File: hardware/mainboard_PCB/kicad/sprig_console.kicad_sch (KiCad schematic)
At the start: 25 parts, among them J1 1020_battery_holder, J2 Conn_PinHeader_2x03_P2.54mm_V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, SW1 W, SW2 A, SW3 S, SW4 D, SW5 I, SW6 J, SW7 K, SW8 L, SW9 Slideswitch, U2 MAX98357AETE+, U5 Pico

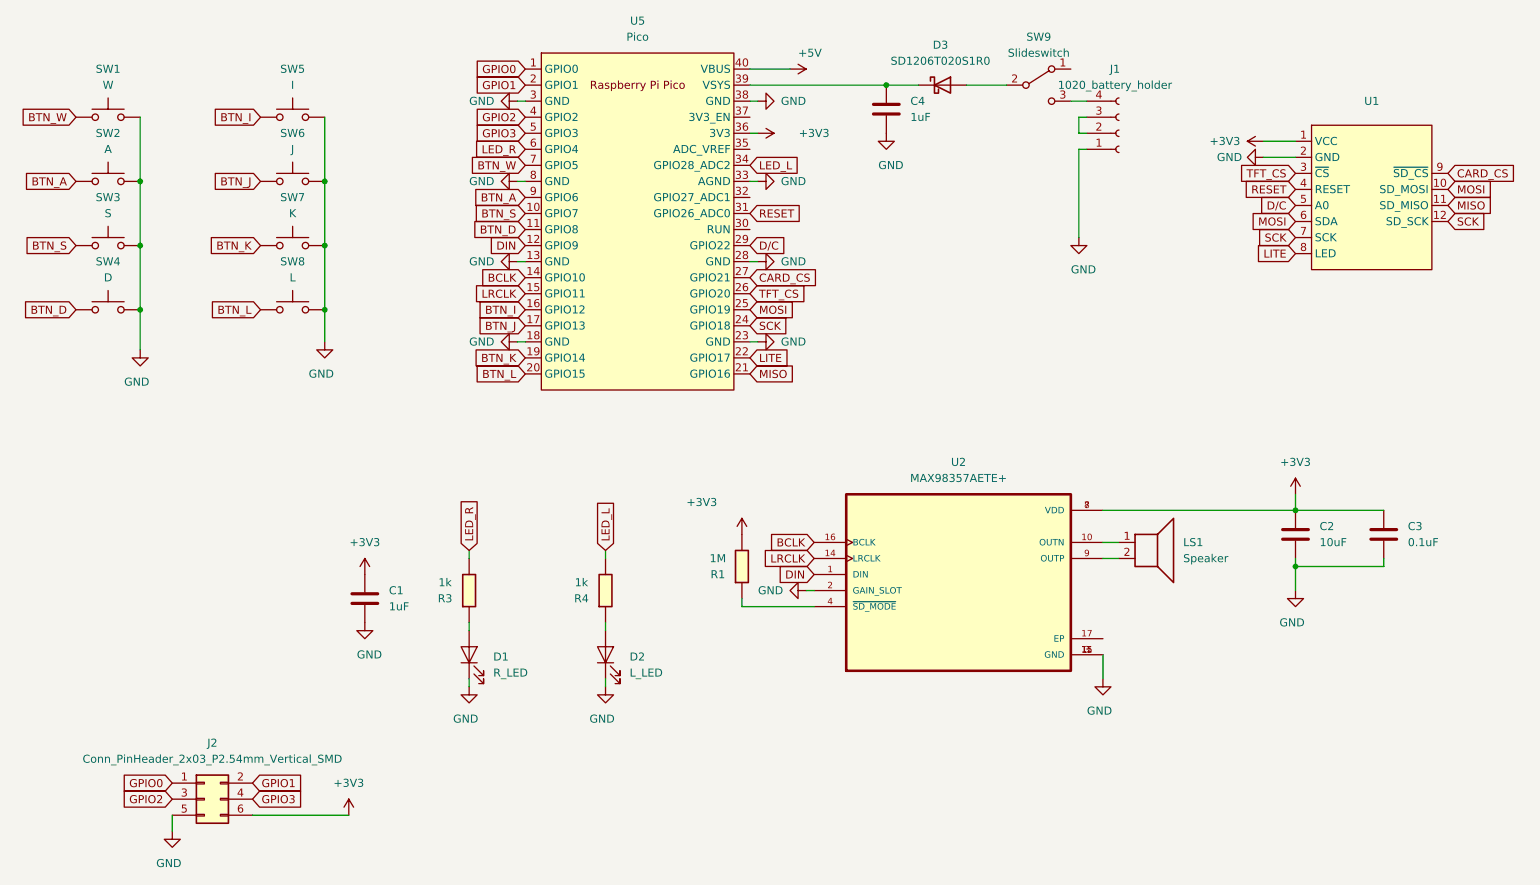
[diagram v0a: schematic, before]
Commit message: temp under screen headers
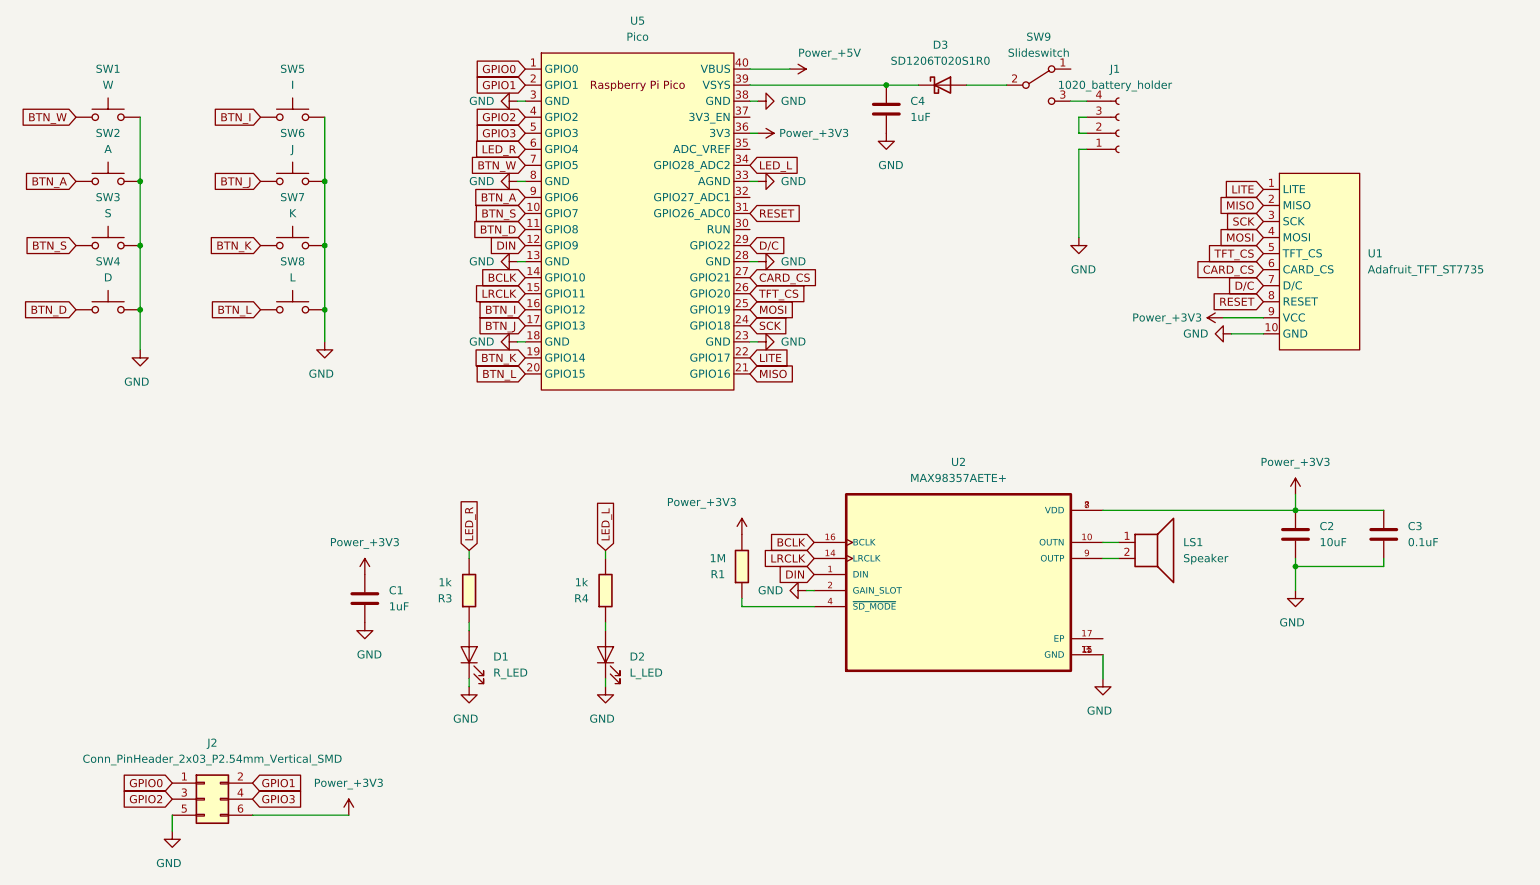
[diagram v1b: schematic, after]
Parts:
- removed U1: ~, sprig:TFT_MSP1803, symbol sprig:TFT_MSP1803
- added U1: Adafruit_TFT_ST7735, fab:TFT_ST7735, symbol fab_custom:Adafruit_TFT_ST7735
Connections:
- net +3V3: now also U1.9 (VCC)
- net CARD_CS: now also U1.6 (CARD_CS)
- net D/C: now also U1.7 (D/C)
- net GND: now also U1.10 (GND)
- net LITE: now also U1.1 (LITE)
- net MISO: now also U1.2 (MISO)
- net MOSI: now also U1.4 (MOSI)
- net RESET: now also U1.8 (RESET)
- net SCK: now also U1.3 (SCK)
- net TFT_CS: now also U1.5 (TFT_CS)

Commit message: new board for new screen (#2430)
* new board design w/ cheaper screens

* new board design w/ cheaper screens

* add nora as co author

Co-authored-by: Nora <nora@hackclub.com>

* try again

wahoo



Co-authored-by: Nora <nora@hackclub.com>

* Update fp-lib-table


Co-authored-by: 24c02 <163450896+24c02@users.noreply.github.com>

---------

Co-authored-by: Nora <nora@hackclub.com>
Co-authored-by: 24c02 <163450896+24c02@users.noreply.github.com>
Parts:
- removed U1: Adafruit_TFT_ST7735, fab:TFT_ST7735, symbol fab_custom:Adafruit_TFT_ST7735
- added U1: ~, sprig:TFT_MSP1803, symbol sprig:TFT_MSP1803
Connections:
- net +3V3: now also U1.1 (VCC)
- net CARD_CS: now also U1.9 (~{SD_CS})
- net D/C: now also U1.5 (A0)
- net GND: now also U1.2 (GND)
- net LITE: now also U1.8 (LED)
- net MISO: now also U1.11 (SD_MISO)
- net MOSI: now also U1.10 (SD_MOSI), U1.6 (SDA)
- net RESET: now also U1.4 (RESET)
- net SCK: now also U1.12 (SD_SCK), U1.7 (SCK)
- net TFT_CS: now also U1.3 (~{CS})
